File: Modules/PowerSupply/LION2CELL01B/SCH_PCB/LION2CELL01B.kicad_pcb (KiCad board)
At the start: 2 copper layers, 80.8 x 60.5 mm, 94 parts, among them J1 JUMP_4X2, J10 JUMP_2x1, J11 JUMP_2x1, J12 JUMP_2x1, J13 JUMP_4X2, J14 JUMP_2x1, J2 JUMP_2x1, J3 JUMP_2x1, J4 JUMP_2x1, J5 JUMP_2x1, J6 JUMP_2x1, J7 JUMP_4X2, J8 CONN1_1, J9 CONN1_1, P1 _, P2 _, P3 _, P4 _, Q1 IRLML6244, Q2 MMBF170LT1G, Q3 MMBF170LT1G, Q4 BSS83P, SW1 SW_PUSH, U1 BQ29209, U2 BQ24103, U3 BQ34Z100, U4 SN74HC164D

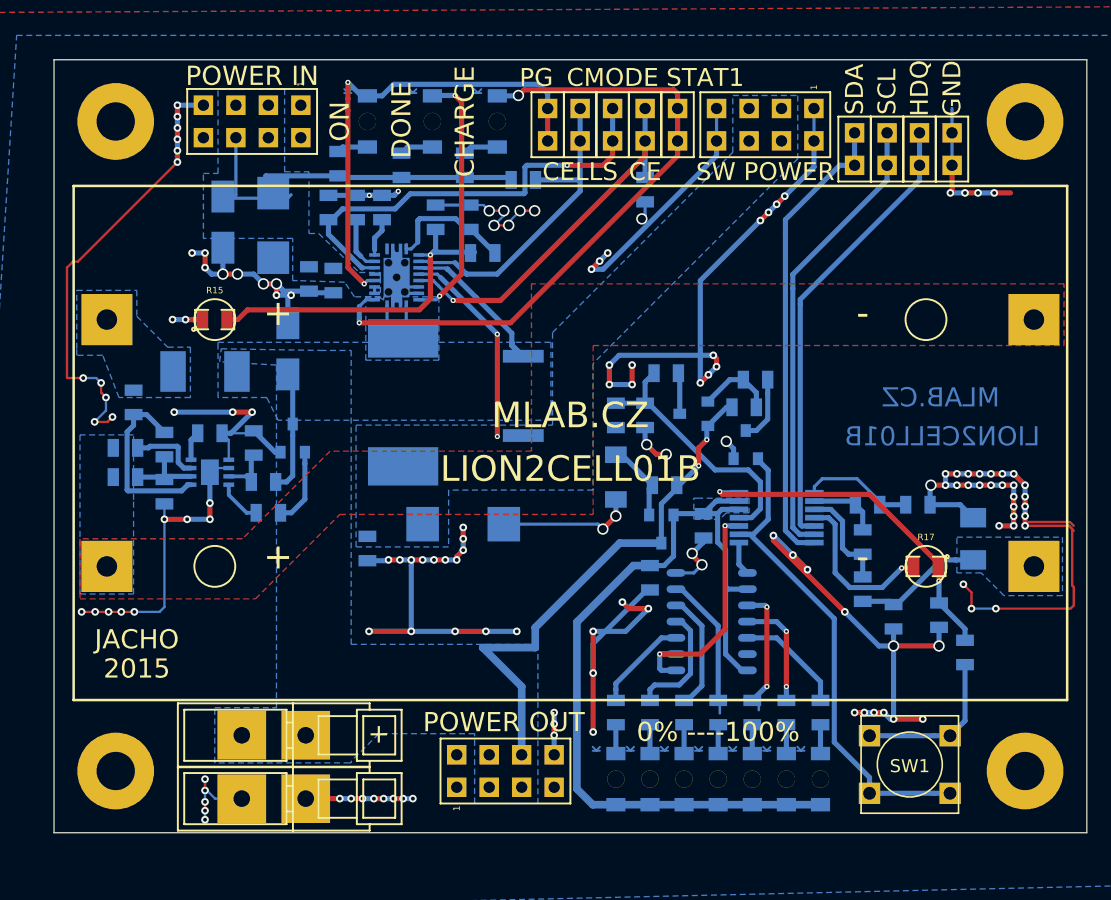
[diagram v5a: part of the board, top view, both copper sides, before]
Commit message: 
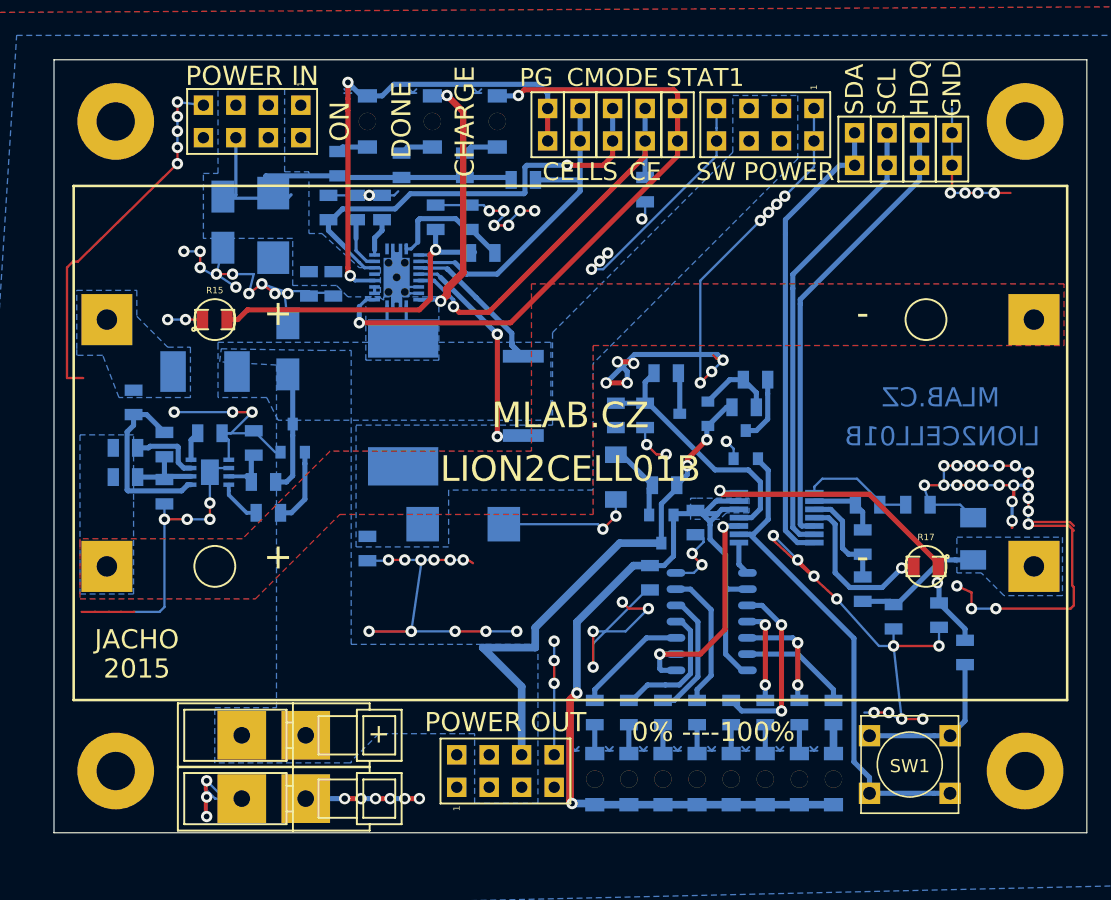
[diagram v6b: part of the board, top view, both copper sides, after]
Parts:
- added D14: ORAGE, Mlab_D:LED_1206, B.Cu at (61.2, -4.45)
- added R34: 1K, Mlab_R:SMD-0805, B.Cu at (61.2, -9.65)
- moved D10 1.65 mm to (50.5, -4.45)
- moved D13 1.65 mm to (58.5, -4.45)
- moved D9 1.65 mm to (47.9, -4.45)
- moved R29 1.65 mm to (47.9, -9.65)
- moved R30 1.65 mm to (50.5, -9.65)
- moved R33 1.65 mm to (58.5, -9.65)
- moved D11 1.65 mm to (53.2, -4.45)
- moved D12 1.65 mm to (55.9, -4.45)
- moved D7 1.65 mm to (42.5, -4.45)
- moved D8 1.65 mm to (45.2, -4.45)
- moved R27 1.65 mm to (42.5, -9.65)
- moved R28 1.65 mm to (45.2, -9.65)
- moved R31 1.65 mm to (53.2, -9.65)
- moved R32 1.65 mm to (55.9, -9.65)
- moved C12 0.68 mm to (50.4, -24.5)
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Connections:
- BT1 pad 2: /BAT-MIDPOINT -> (no net)
- U4 pad 13: (no net) -> Net-(R34-Pad2)
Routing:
- net Net-(R34-Pad2): track 0.00 -> 8.72 mm
- net GND: track 389.4 -> 395.9 mm, vias 145 -> 117
- net Net-(R31-Pad2): track 10.0 -> 14.7 mm
- net /REGIN: track 69.3 -> 73.9 mm, vias 0 -> 2
- net (no net): track 0.00 -> 4.12 mm
- net Net-(D14-Pad2): track 0.00 -> 2.25 mm
- net Net-(R32-Pad2): track 8.76 -> 7.41 mm
- net Net-(R28-Pad2): track 9.32 -> 10.5 mm
- net Net-(R27-Pad2): track 7.76 -> 8.87 mm
- net /CE: track 29.6 -> 30.7 mm
- net Net-(R29-Pad2): track 9.25 -> 10.0 mm
- net Net-(R13-Pad1): track 26.3 -> 26.9 mm
- net Net-(R33-Pad2): track 8.60 -> 8.66 mm, vias 0 -> 2
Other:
- net class Default: via_dia 0.4 -> 0.89; via_drill 0.3 -> 0.5
- rule via_min_drill: 0.3 -> 0.5
- rule via_min_size: 0.3 -> 0.89
